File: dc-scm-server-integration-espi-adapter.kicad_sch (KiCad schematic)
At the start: 2 parts

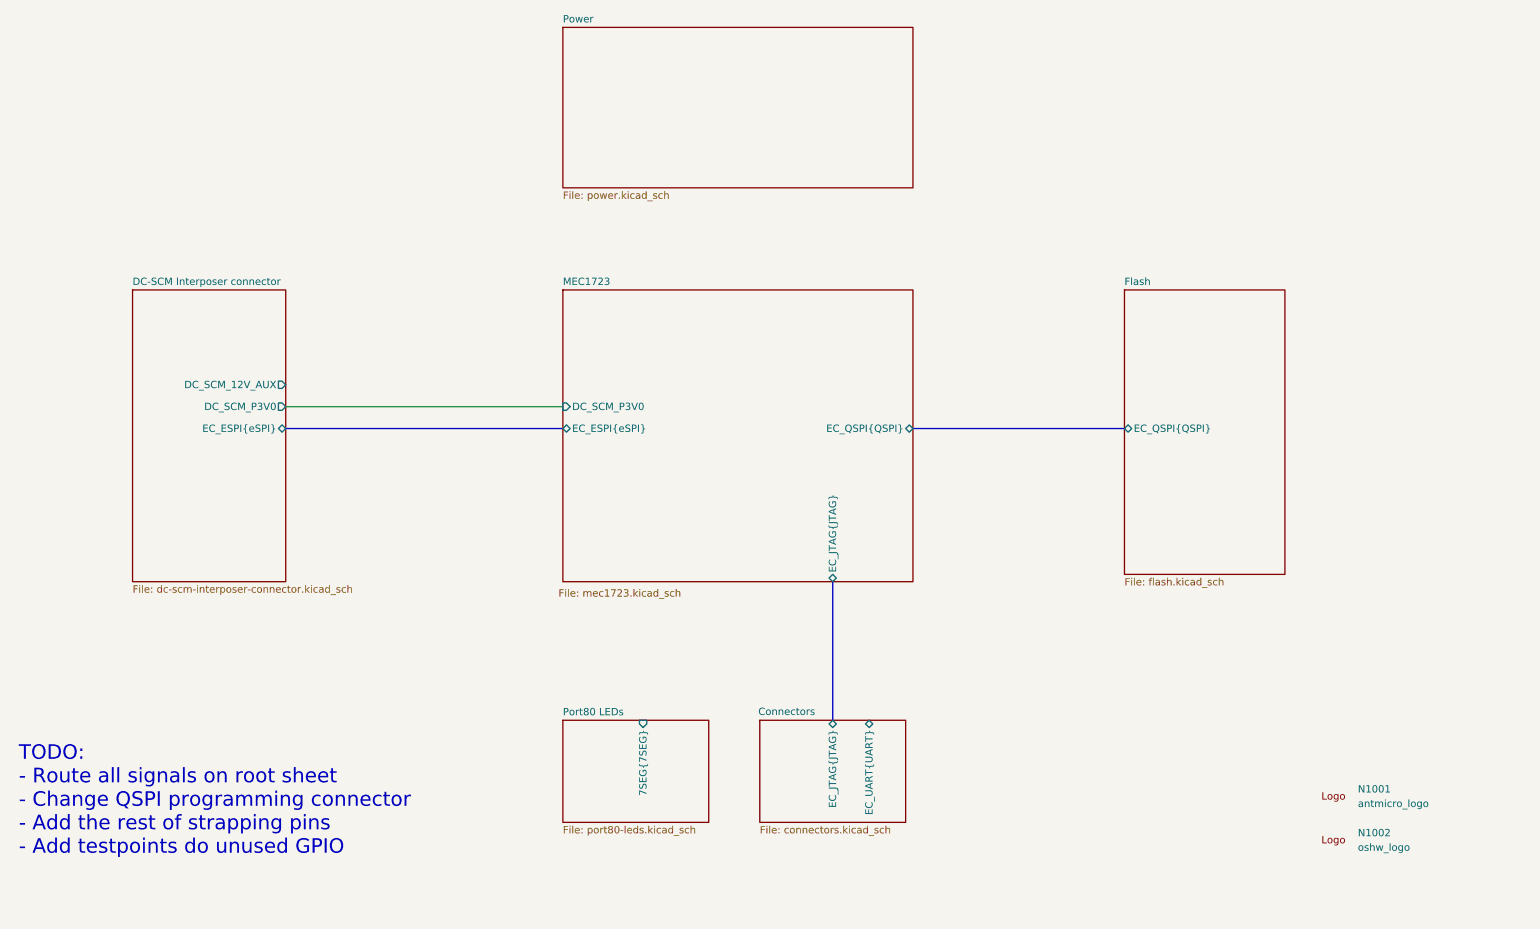
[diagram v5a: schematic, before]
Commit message: [#103224] Divide 7SEG bus into 2, rename JTAG connector pins
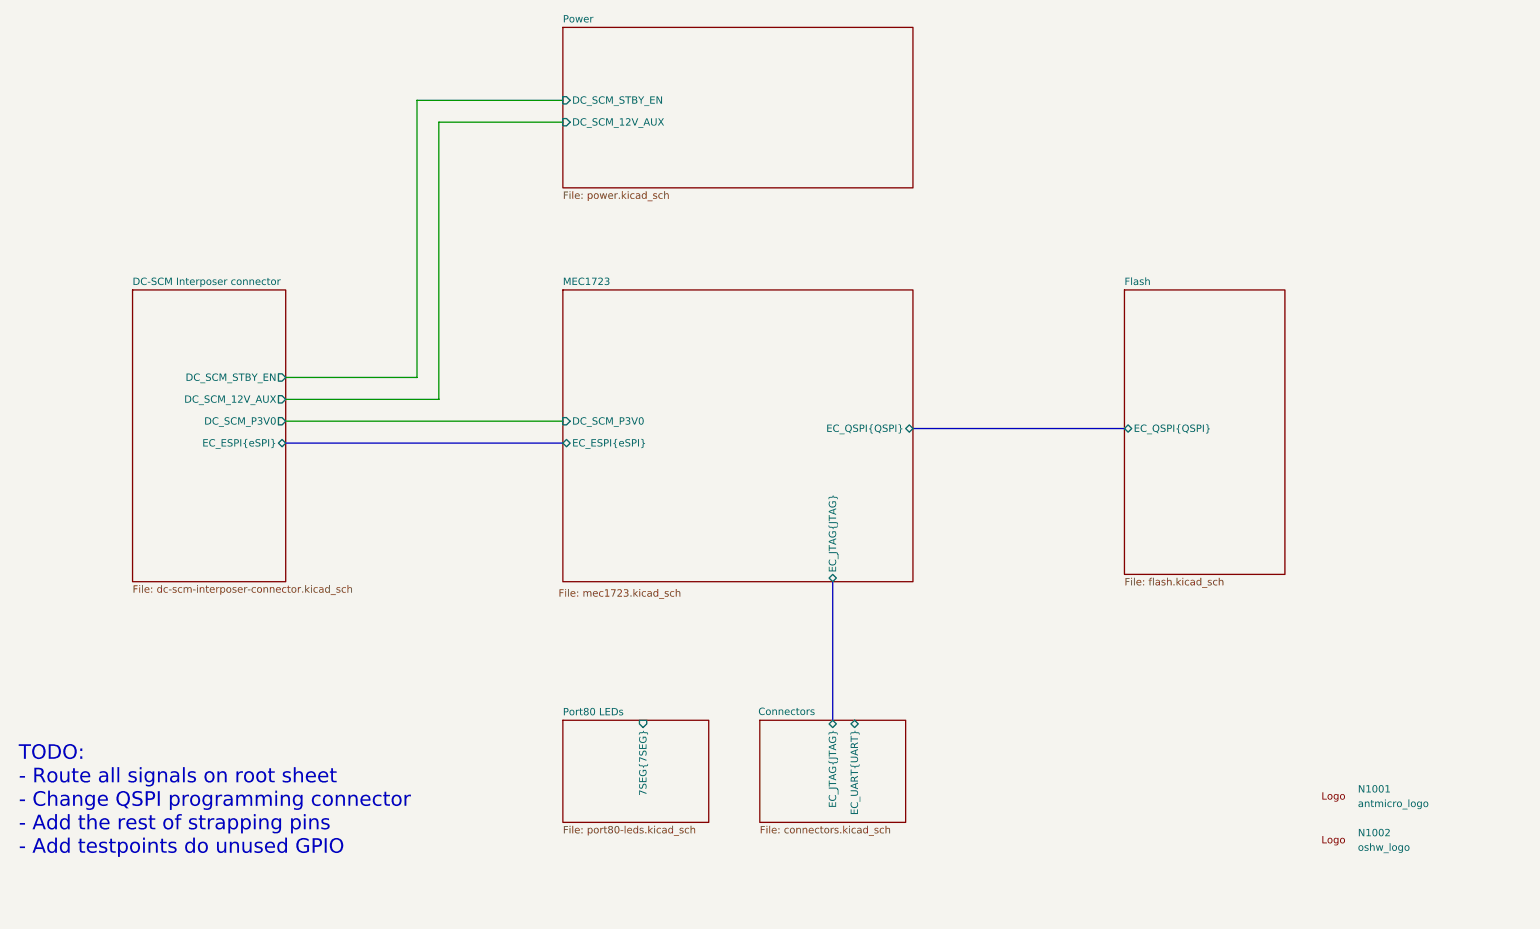
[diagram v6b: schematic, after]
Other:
- sheet DC-SCM Interposer connector ports: added DC_SCM_STBY_EN; removed none
- sheet Power ports: added DC_SCM_12V_AUX, DC_SCM_STBY_EN; removed none
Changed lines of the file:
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@@
 			(font
 				(size 2.54 2.54)
-				(color 255 6 32 1)
 			)
 			(justify left)
@@
 		)
 	)
+	(wire
+		(pts
+			(xy 69.85 85.09) (xy 96.52 85.09)
+		)
+		(stroke
+			(width 0)
+			(type default)
+		)
+	)
+	(wire
+		(pts
+			(xy 96.52 36.83) (xy 118.11 36.83)
+		)
+		(stroke
+			(width 0)
+			(type default)
+		)
+	)
+	(wire
+		(pts
+			(xy 96.52 85.09) (xy 96.52 36.83)
+		)
+		(stroke
+			(width 0)
+			(type default)
+		)
+	)
 	(bus
 		(pts
@@
 	(wire
 		(pts
-			(xy 69.85 86.36) (xy 118.11 86.36)
+			(xy 69.85 88.9) (xy 118.11 88.9)
+		)
+		(stroke
+			(width 0)
+			(type default)
+		)
+	)
+	(wire
+		(pts
+			(xy 69.85 81.28) (xy 92.71 81.28)
+		)
+		(stroke
+			(width 0)
+			(type default)
+		)
+	)
+	(wire
+		(pts
+			(xy 92.71 33.02) (xy 118.11 33.02)
 		)
 		(stroke
@@
 	(bus
 		(pts
-			(xy 69.85 90.17) (xy 118.11 90.17)
+			(xy 69.85 92.71) (xy 118.11 92.71)
+		)
+		(stroke
+			(width 0)
+			(type default)
+		)
+	)
+	(wire
+		(pts
+			(xy 92.71 81.28) (xy 92.71 33.02)
 		)
 		(stroke
@@
 			)
 		)
+		(pin "DC_SCM_12V_AUX" input
+			(at 118.11 36.83 180)
+			(effects
+				(font
+					(size 1.27 1.27)
+				)
+				(justify left)
+			)
+		)
+		(pin "DC_SCM_STBY_EN" input
+			(at 118.11 33.02 180)
+			(effects
+				(font
+					(size 1.27 1.27)
+				)
+				(justify left)
+			)
+		)
 		(instances
 			(project "dc-scm-server-integration-espi-adapter"
@@
 		)
 		(pin "EC_UART{UART}" bidirectional
-			(at 171.45 140.97 90)
+			(at 168.91 140.97 90)
 			(effects
 				(font
@@
 		)
 		(pin "EC_ESPI{eSPI}" bidirectional
-			(at 118.11 90.17 180)
+			(at 118.11 92.71 180)
 			(effects
 				(font
@@
 		)
 		(pin "DC_SCM_P3V0" input
-			(at 118.11 86.36 180)
+			(at 118.11 88.9 180)
 			(effects
 				(font
@@
 		)
 		(pin "DC_SCM_12V_AUX" output
-			(at 69.85 82.55 0)
+			(at 69.85 85.09 0)
 			(effects
 				(font
@@
 		)
 		(pin "EC_ESPI{eSPI}" bidirectional
-			(at 69.85 90.17 0)
+			(at 69.85 92.71 0)
 			(effects
 				(font
@@
 		)
 		(pin "DC_SCM_P3V0" output
-			(at 69.85 86.36 0)
-			(effects
-				(font
+			(at 69.85 88.9 0)
+			(effects
+				(font
+					(size 1.27 1.27)
+				)
+				(justify right)
+			)
+		)
+		(pin "DC_SCM_STBY_EN" output
+			(at 69.85 81.28 0)
+			(effects
+				(font

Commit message: [#103224] Add root schematic connections, add EMDRST button, add 1u decoupling capacitors, connect UART, add fiducials
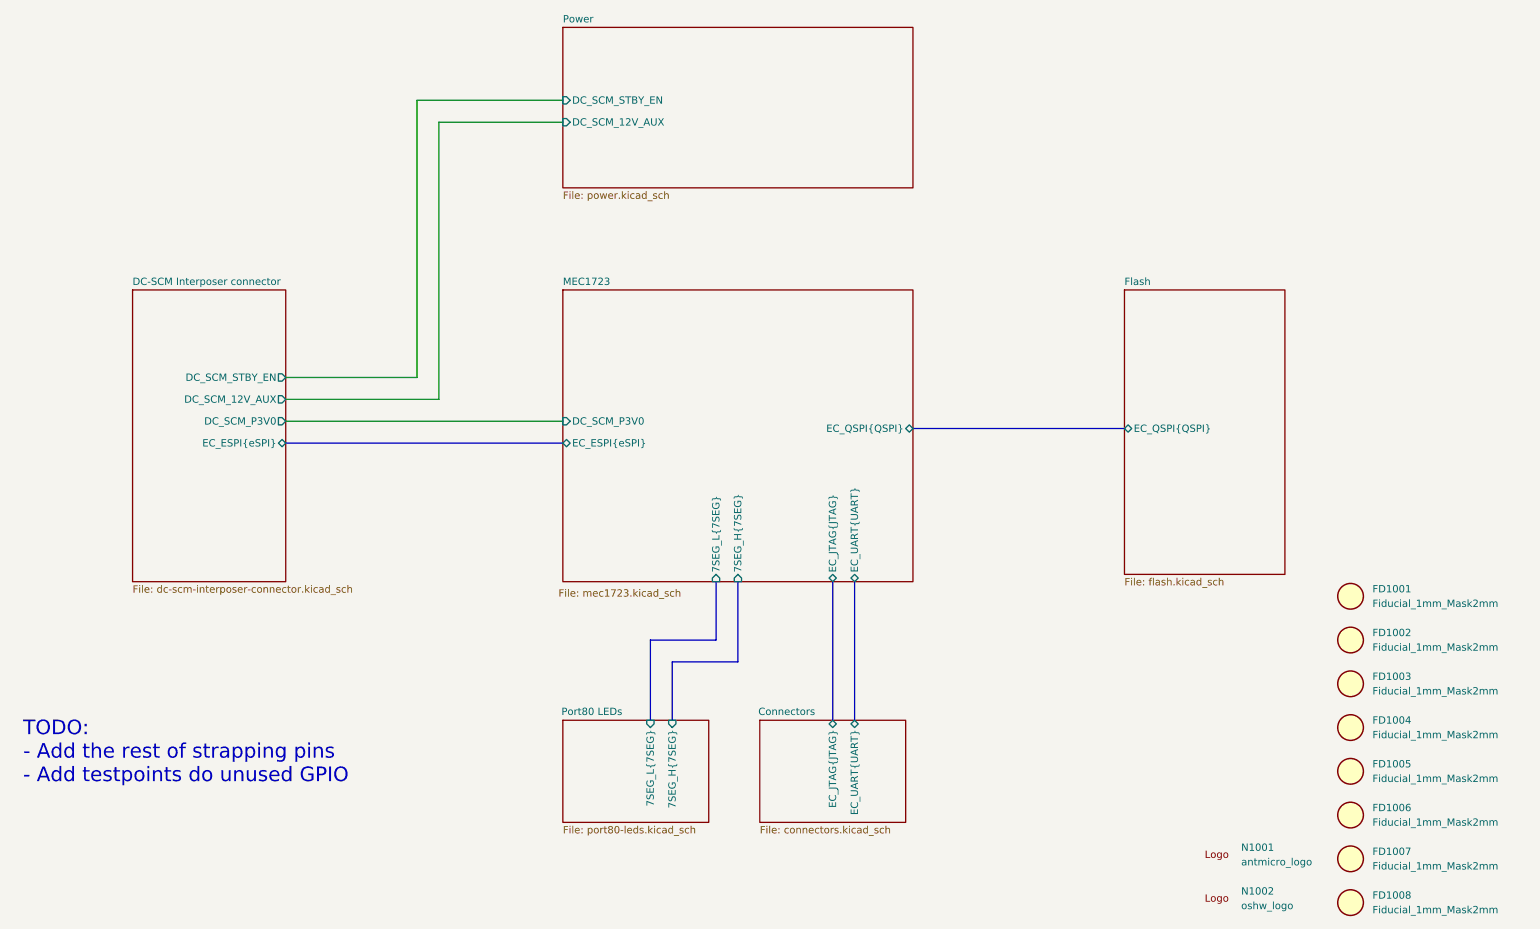
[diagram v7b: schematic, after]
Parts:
- added FD1001, FD1002, FD1003, FD1004, FD1005, FD1006, FD1007, FD1008: Fiducial_1mm_Mask2mm, antmicro-footprints:Fiducial_1mm_Mask2mm, symbol Antmicro Symbols:Fiducial_1mm_Mask2mm
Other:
- sheet MEC1723 ports: added 7SEG_H{7SEG}, 7SEG_L{7SEG}, EC_UART{UART}; removed none
- sheet Port80 LEDs ports: added 7SEG_H{7SEG}, 7SEG_L{7SEG}; removed 7SEG{7SEG}
- note added: "TODO: - Add the rest of strapping pins - Add testpoints do unused GPIO"
- note removed: "TODO: - Route all signals on root sheet - Change QSPI programming connector - Add the rest of strapping pins - Add testpoints do unused GPIO"
- moved on the sheet: N1001, N1002

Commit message: [#103224] Add UART1, added GND to breakout connectors, fix orientation of DC-SCM connector, delete unused notes
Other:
- sheet Connectors ports: added EC_UART0{UART}, EC_UART1{UART}; removed EC_UART{UART}
- sheet MEC1723 ports: added EC_UART0{UART}, EC_UART1{UART}; removed EC_UART{UART}
- note removed: "TODO: - Add the rest of strapping pins - Add testpoints do unused GPIO"
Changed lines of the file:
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@@
 		(comment 1 "www.antmicro.com")
 	)
-	(text "TODO:\n- Add the rest of strapping pins\n- Add testpoints do unused GPIO"
-		(exclude_from_sim no)
-		(at 24.13 146.558 0)
-		(effects
-			(font
-				(size 2.54 2.54)
-			)
-			(justify left)
-		)
-	)
 	(bus
 		(pts
@@
 		)
 	)
+	(wire
+		(pts
+			(xy 69.85 85.09) (xy 96.52 85.09)
+		)
+		(stroke
+			(width 0)
+			(type default)
+		)
+	)
 	(bus
 		(pts
+			(xy 144.78 116.84) (xy 144.78 127)
+		)
+		(stroke
+			(width 0)
+			(type default)
+		)
+	)
+	(wire
+		(pts
+			(xy 96.52 36.83) (xy 118.11 36.83)
+		)
+		(stroke
+			(width 0)
+			(type default)
+		)
+	)
+	(wire
+		(pts
+			(xy 96.52 85.09) (xy 96.52 36.83)
+		)
+		(stroke
+			(width 0)
+			(type default)
+		)
+	)
+	(bus
+		(pts
+			(xy 165.1 116.84) (xy 165.1 140.97)
+		)
+		(stroke
+			(width 0)
+			(type default)
+		)
+	)
+	(bus
+		(pts
 			(xy 168.91 116.84) (xy 168.91 140.97)
 		)
@@
 	(wire
 		(pts
-			(xy 69.85 85.09) (xy 96.52 85.09)
+			(xy 69.85 88.9) (xy 118.11 88.9)
+		)
+		(stroke
+			(width 0)
+			(type default)
+		)
+	)
+	(wire
+		(pts
+			(xy 69.85 81.28) (xy 92.71 81.28)
 		)
 		(stroke
@@
 	(bus
 		(pts
-			(xy 144.78 116.84) (xy 144.78 127)
+			(xy 144.78 127) (xy 133.35 127)
+		)
+		(stroke
+			(width 0)
+			(type default)
+		)
+	)
+	(bus
+		(pts
+			(xy 148.59 130.81) (xy 148.59 116.84)
 		)
 		(stroke
@@
 	(wire
 		(pts
-			(xy 96.52 36.83) (xy 118.11 36.83)
-		)
-		(stroke
-			(width 0)
-			(type default)
-		)
-	)
-	(wire
-		(pts
-			(xy 96.52 85.09) (xy 96.52 36.83)
+			(xy 92.71 33.02) (xy 118.11 33.02)
 		)
 		(stroke
@@
 	(bus
 		(pts
-			(xy 165.1 116.84) (xy 165.1 140.97)
-		)
-		(stroke
-			(width 0)
-			(type default)
-		)
-	)
-	(wire
-		(pts
-			(xy 69.85 88.9) (xy 118.11 88.9)
-		)
-		(stroke
-			(width 0)
-			(type default)
-		)
-	)
-	(wire
-		(pts
-			(xy 69.85 81.28) (xy 92.71 81.28)
+			(xy 69.85 92.71) (xy 118.11 92.71)
 		)
 		(stroke
@@
 	(bus
 		(pts
-			(xy 144.78 127) (xy 133.35 127)
-		)
-		(stroke
-			(width 0)
-			(type default)
-		)
-	)
-	(bus
-		(pts
-			(xy 148.59 130.81) (xy 148.59 116.84)
-		)
-		(stroke
-			(width 0)
-			(type default)
-		)
-	)
-	(wire
-		(pts
-			(xy 92.71 33.02) (xy 118.11 33.02)
-		)
-		(stroke
-			(width 0)
-			(type default)
-		)
-	)
-	(bus
-		(pts
-			(xy 69.85 92.71) (xy 118.11 92.71)
+			(xy 172.72 116.84) (xy 172.72 140.97)
 		)
 		(stroke
@@
 			)
 		)
-		(pin "EC_UART{UART}" bidirectional
+		(pin "EC_UART0{UART}" bidirectional
 			(at 168.91 140.97 90)
+			(effects
+				(font
+					(size 1.27 1.27)
+				)
+				(justify right)
+			)
+		)
+		(pin "EC_UART1{UART}" bidirectional
+			(at 172.72 140.97 90)
 			(effects
 				(font
@@
 			)
 		)
-		(pin "7SEG_H{7SEG}" input
+		(pin "EC_UART0{UART}" bidirectional
+			(at 168.91 116.84 270)
+			(effects
+				(font
+					(size 1.27 1.27)
+				)
+				(justify left)
+			)
+		)
+		(pin "EC_UART1{UART}" bidirectional
+			(at 172.72 116.84 270)
+			(effects
+				(font
+					(size 1.27 1.27)
+				)
+				(justify left)
+			)
+		)
+		(pin "7SEG_H{7SEG}" output
+			(at 144.78 116.84 270)
+			(effects
+				(font
+					(size 1.27 1.27)
+				)
+				(justify left)
+			)
+		)
+		(pin "7SEG_L{7SEG}" output
 			(at 148.59 116.84 270)
 			(effects
 				(font
-					(size 1.27 1.27)
-				)
-				(justify left)
-			)
-		)
-		(pin "7SEG_L{7SEG}" input
-			(at 144.78 116.84 270)
-			(effects
-				(font
-					(size 1.27 1.27)
-				)
-				(justify left)
-			)
-		)
-		(pin "EC_UART{UART}" bidirectional
-			(at 168.91 116.84 270)
-			(effects
-				(font
